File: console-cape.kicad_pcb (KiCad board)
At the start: 2 copper layers, 101.6 x 66.1 mm, 22 parts, among them J1 LCD HEADER, J2 FTDI, J3 ISP-2560, J4 DIGOUT1, J5 DIGOUT2, J6 LCD TEST, J7 CONN_01X02, U2 ATMEGA328, X1 16MHz 18pF

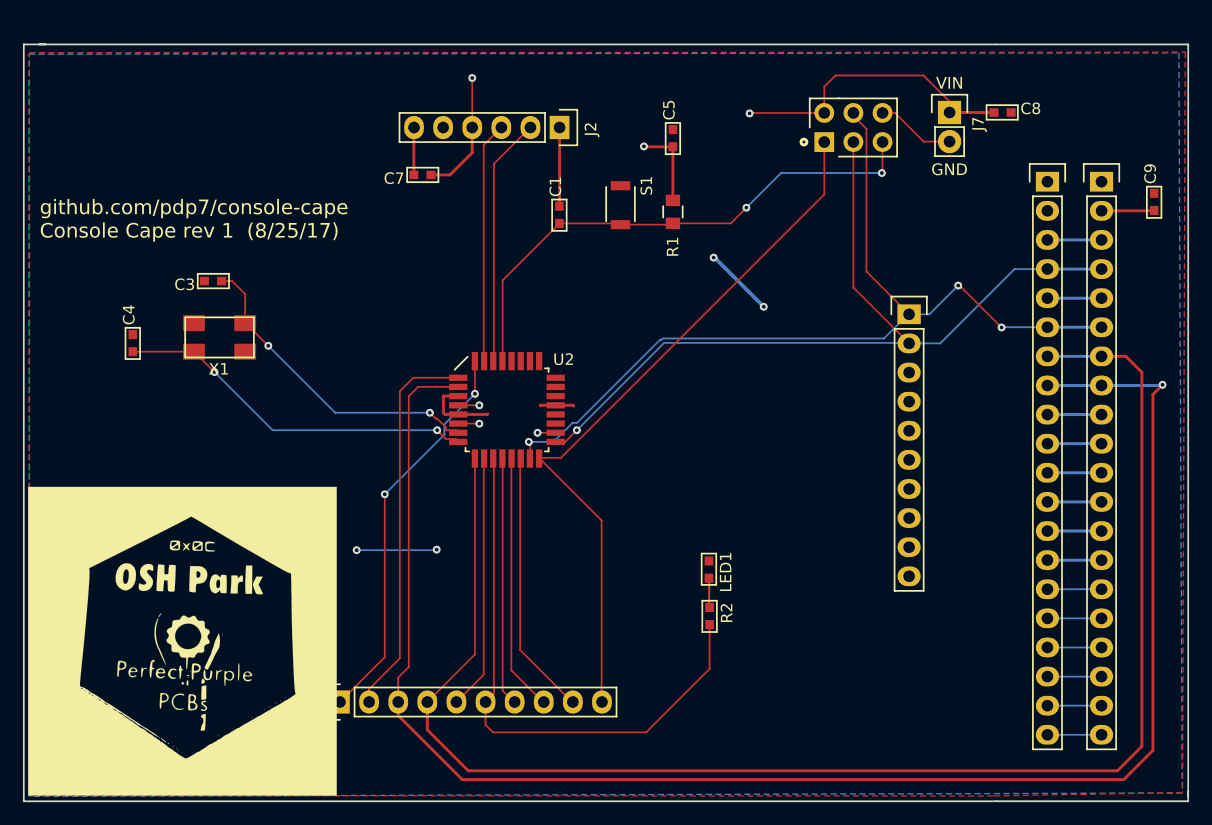
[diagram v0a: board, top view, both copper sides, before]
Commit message: clean up traces on top and bottom copper
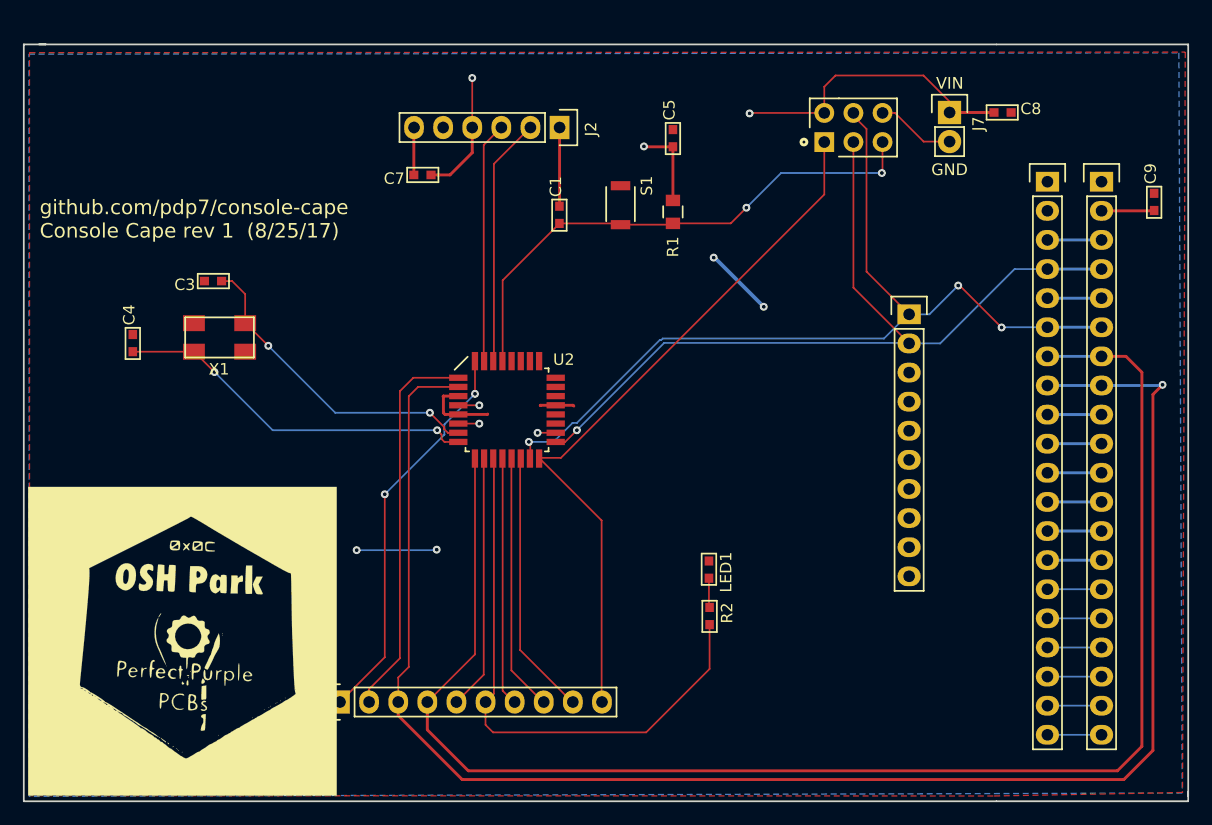
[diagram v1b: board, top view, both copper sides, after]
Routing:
- net (no net): track 15.9 -> 13.3 mm

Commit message: added header to get GND and 3V3 from BBB P9
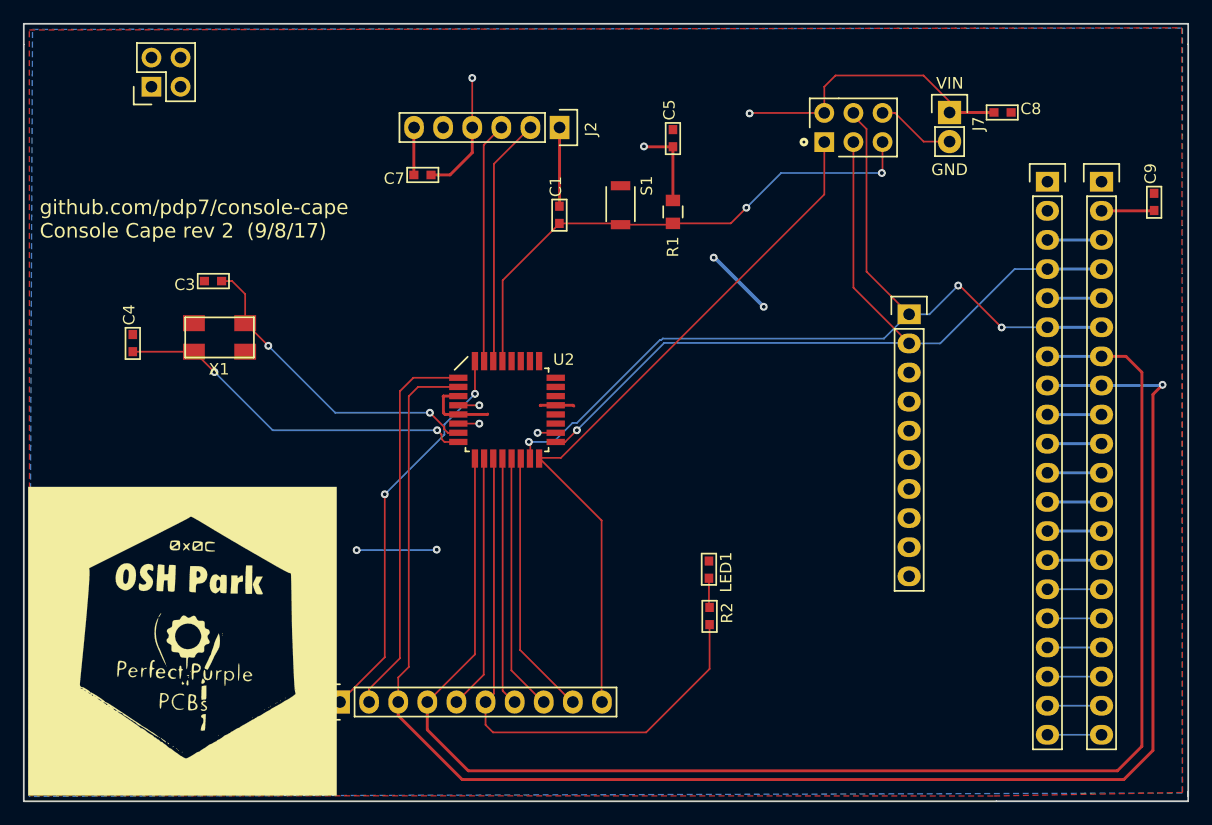
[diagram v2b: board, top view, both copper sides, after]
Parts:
- added J8: CONN_02X02, Wickerlib:CONN-HEADER-STRAIGHT-P2.54MM-2x02, F.Cu at (135.6, 54.1)
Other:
- board size 101.6 x 66.1 mm -> 101.6 x 67.8 mm
- board text added: "github.com/pdp7/console-cape Console Cape rev 2 (9/8/17)"
- board text removed: "github.com/pdp7/console-cape Console Cape rev 1 (8/25/17)"
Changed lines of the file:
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@@
 (kicad_pcb (version 4) (host pcbnew 4.0.6)
   (general
-    (links 78)
+    (links 82)
     (no_connects 0)
-    (area 124.383799 50.323799 226.141281 116.526201)
+    (area 124.383799 48.533799 226.141281 116.526201)
     (thickness 1.6)
-    (drawings 14)
+    (drawings 13)
     (tracks 288)
     (zones 0)
-    (modules 22)
+    (modules 23)
     (nets 55)
   )
@@
       (xy 0.074814 -8.51879) (xy 0.078664 -8.570686) (xy 0.146572 -8.549502)) (layer F.SilkS) (width 0.01))
   )
-  (gr_text "github.com/pdp7/console-cape\nConsole Cape rev 1  (8/25/17)\n\n" (at 163.449 66.72072) (layer B.SilkS)
+  (module Wickerlib:CONN-HEADER-STRAIGHT-P2.54MM-2x02 (layer F.Cu)
+    (at 135.6 54.1 90)
+    (descr "Through hole pin header")
+    (tags "pin header")
+    (fp_text reference J8 (at 1.25 1.25 90) (layer F.Fab)
+      (effects (font (size 1 1) (thickness 0.15)))
+    )
+    (fp_text value CONN_02X02 (at 0 -3.1 90) (layer F.Fab) hide
+      (effects (font (size 1 1) (thickness 0.15)))
+    )
+    (fp_line (start -1.75 -1.75) (end -1.75 4.3) (layer F.Fab) (width 0.05))
+    (fp_line (start 4.3 -1.75) (end 4.3 4.3) (layer F.Fab) (width 0.05))
+    (fp_line (start -1.75 -1.75) (end 4.3 -1.75) (layer F.Fab) (width 0.05))
+    (fp_line (start -1.75 4.3) (end 4.3 4.3) (layer F.Fab) (width 0.05))
+    (fp_line (start -1.75 -1.75) (end -1.75 4.3) (layer F.CrtYd) (width 0.05))
+    (fp_line (start 4.3 -1.75) (end 4.3 4.3) (layer F.CrtYd) (width 0.05))
+    (fp_line (start -1.75 -1.75) (end 4.3 -1.75) (layer F.CrtYd) (width 0.05))
+    (fp_line (start -1.75 4.3) (end 4.3 4.3) (layer F.CrtYd) (width 0.05))
+    (fp_line (start -1.55 0) (end -1.55 -1.55) (layer F.SilkS) (width 0.15))
+    (fp_line (start 0 -1.55) (end -1.55 -1.55) (layer F.SilkS) (width 0.15))
+    (fp_line (start -1.27 1.27) (end 1.27 1.27) (layer F.SilkS) (width 0.15))
+    (fp_line (start 1.27 1.27) (end 1.27 -1.27) (layer F.SilkS) (width 0.15))
+    (fp_line (start 1.27 -1.27) (end 3.81 -1.27) (layer F.SilkS) (width 0.15))
+    (fp_line (start 3.81 -1.27) (end 3.81 3.81) (layer F.SilkS) (width 0.15))
+    (fp_line (start 3.81 3.81) (end -1.27 3.81) (layer F.SilkS) (width 0.15))
+    (fp_line (start -1.27 3.81) (end -1.27 1.27) (layer F.SilkS) (width 0.15))
+    (pad 1 thru_hole rect (at 0 0 90) (size 1.7272 1.7272) (drill 1.016) (layers *.Cu *.Mask F.SilkS)
+      (net 3 GND))
+    (pad 2 thru_hole oval (at 2.54 0 90) (size 1.7272 1.7272) (drill 1.016) (layers *.Cu *.Mask F.SilkS)
+      (net 3 GND))
+    (pad 3 thru_hole oval (at 0 2.54 90) (size 1.7272 1.7272) (drill 1.016) (layers *.Cu *.Mask F.SilkS)
+      (net 35 VIN))
+    (pad 4 thru_hole oval (at 2.54 2.54 90) (size 1.7272 1.7272) (drill 1.016) (layers *.Cu *.Mask F.SilkS)
+      (net 35 VIN))
+  )
+  (gr_line (start 226.06 48.61) (end 226.06 50.41) (angle 90) (layer Edge.Cuts) (width 0.1524))
+  (gr_line (start 124.46 48.61) (end 226.06 48.61) (angle 90) (layer Edge.Cuts) (width 0.1524))
+  (gr_line (start 124.46 50.42) (end 124.46 48.61) (angle 90) (layer Edge.Cuts) (width 0.1524))
+  (gr_text "github.com/pdp7/console-cape\nConsole Cape rev 2 (9/8/17)\n\n" (at 163.449 66.72072) (layer B.SilkS)
     (effects (font (thickness 0.1778)) (justify left mirror))
   )
-  (gr_text "github.com/pdp7/console-cape\nConsole Cape rev 1  (8/25/17)\n\n" (at 125.8443 66.675) (layer F.SilkS)
+  (gr_text "github.com/pdp7/console-cape\nConsole Cape rev 2  (9/8/17)\n\n" (at 125.8443 66.675) (layer F.SilkS)
     (effects (font (thickness 0.1778)) (justify left))
   )
@@
   (gr_line (start 209.31632 116.44884) (end 226.05746 116.44884) (angle 90) (layer Edge.Cuts) (width 0.1524))
   (gr_line (start 226.06254 50.41138) (end 226.06254 115.99926) (angle 90) (layer Edge.Cuts) (width 0.1524))
-  (gr_line (start 209.3341 50.41138) (end 226.06254 50.41138) (angle 90) (layer Edge.Cuts) (width 0.1524))
   (gr_text GND (at 205.24 61.34) (layer F.SilkS)
     (effects (font (size 1.016 1.016) (thickness 0.1524)))
@@
     (effects (font (size 1.016 1.016) (thickness 0.1524)))
   )
-  (gr_line (start 126.36 50.41) (end 126.36 50.4) (angle 90) (layer Edge.Cuts) (width 0.1524))
-  (gr_line (start 124.46 50.41) (end 126.36 50.41) (angle 90) (layer Edge.Cuts) (width 0.1524))
   (gr_line (start 124.46 116.45) (end 124.46 50.41) (angle 90) (layer Edge.Cuts) (width 0.1524))
   (gr_line (start 209.3 116.45) (end 124.46 116.45) (angle 90) (layer Edge.Cuts) (width 0.1524))
-  (gr_line (start 125.79 50.41) (end 209.3 50.41) (angle 90) (layer Edge.Cuts) (width 0.1524))
   (via (at 160.48736 94.49308) (size 0.6858) (drill 0.3302) (layers F.Cu B.Cu) (net 0))
   (via (at 153.5049 94.5388) (size 0.6858) (drill 0.3302) (layers F.Cu B.Cu) (net 0))
@@
     (polygon
       (pts
-        (xy 124.9553 51.1302) (xy 225.806 51.0794) (xy 225.5647 115.6843) (xy 209.06 115.99) (xy 124.9616 115.9632)
+        (xy 124.94 49.15) (xy 225.506 48.9594) (xy 225.5647 115.6843) (xy 209.06 115.99) (xy 124.9616 115.9632)
       )
     )
@@
     (polygon
       (pts
-        (xy 124.91 51.26) (xy 225.2472 51.1429) (xy 225.5456 115.7303) (xy 124.9299 116.0272)
+        (xy 125.22 49.1) (xy 225.5572 48.9829) (xy 225.5456 115.7303) (xy 124.9299 116.0272)
       )
     )
